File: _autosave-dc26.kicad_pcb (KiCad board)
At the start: 4 copper layers, 129.2 x 142.3 mm, 694 parts, among them J1 CONN_01X10, J2 CONN_01X10, J3 CONN_01X10, Q1 IRLB8721PBF, Y1 Crystal

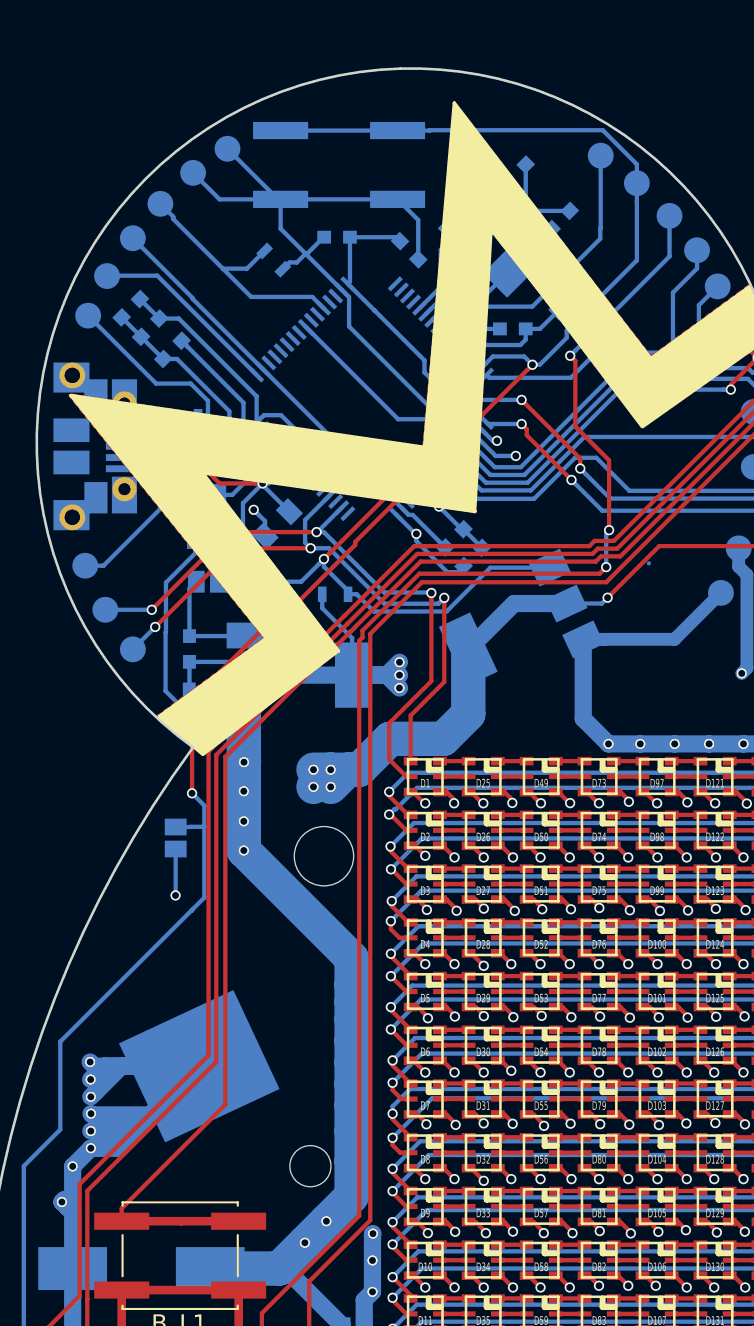
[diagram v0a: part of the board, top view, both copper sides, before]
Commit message: Name changes on silk
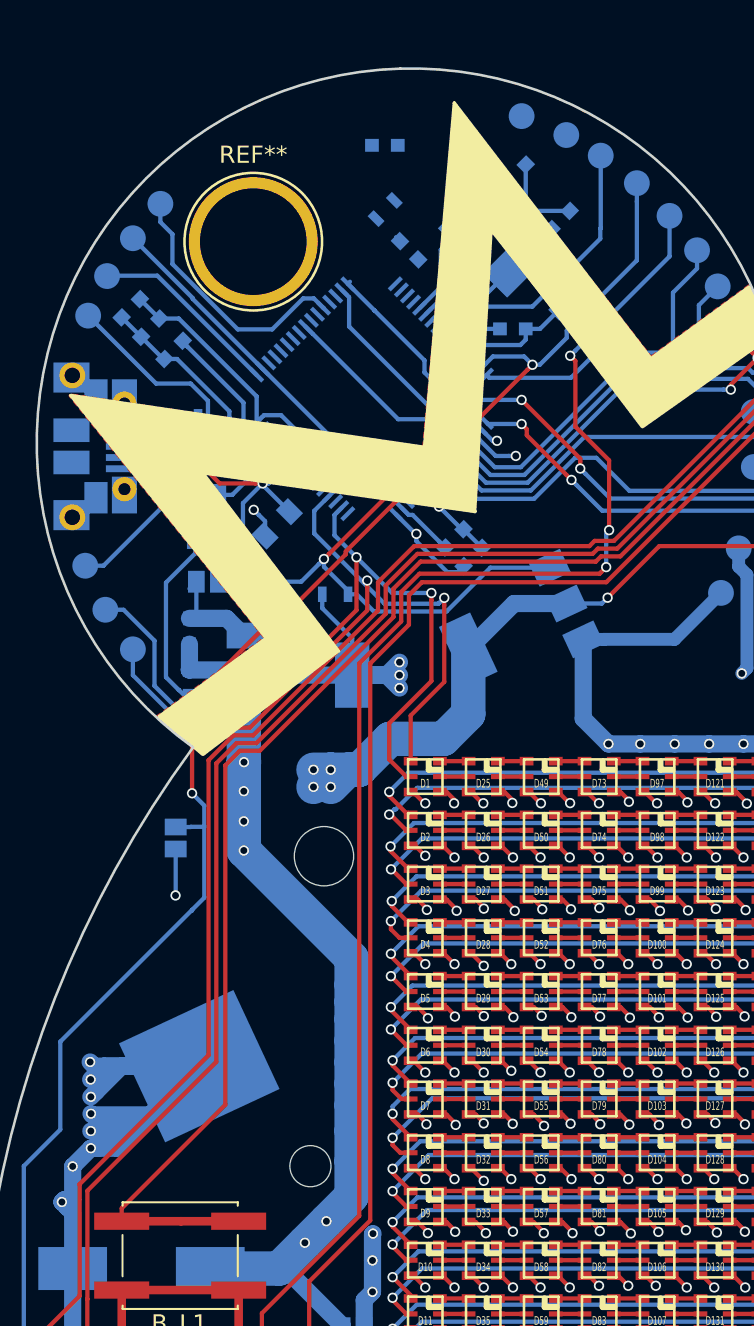
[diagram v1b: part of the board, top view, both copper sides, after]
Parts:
- removed SW_PWRON1: SW_SPST, Buttons_Switches_SMD:SW_SPST_EVQQ2
- added REF**: 1pin, custom-footprints:1pin-7mm, F.Cu at (126.5, 65.3)
- moved LGND1 19.7 mm to (144.7, 59.1)
- moved PGND1 19.4 mm to (142.1, 58.0)
- moved R14 7.12 mm to (134.2, 63.4), turned to 45 degrees
- moved C28 6.02 mm to (134.2, 59.7)
- moved C33 1.13 mm to (122.8, 91.0)
- moved C29 1.03 mm to (122.8, 88.0)
- moved C27 0.07 mm to (121.9, 71.6)
- turned NRST1 to 0 degrees
- renumbered TP-BATT-BUCK-ENABLE1 to BBEN1, TP-BTN-CLK1 to BCLK1, TP-BTN-DATA1 to BDATA1, TP-BATT-GND1 to BGND1, TP-BTN-GND1 to BGND2, TP-BATT-IN1 to BIN1, TP-BTN-LOAD1 to BLD1, TP-BOOT0 to BT0, JMP-BATT-BUCK-ENABLE1 to JBBEN1, JMP-LED-PWR-EN-BYP1 to JLEN1, JMP-LED-PWR-BYP1 to JLPWR1, JMP-USBID1 to JUID1, JMP-USBVCC1 to JUVCC1, TP-LED-CKI1 to LCKI1, TP-LED-PWR-EN1 to LEN1, TP-LED-GND1 to LGND1, TP-LED-SDI1 to LSDI1, TP-LED-VCC1 to LVCC1, TP-MPU6000-CS1 to MCS1, TP-MPU6000-INT1 to MINT1, TP-MPU6000-MISO1 to MMISO1, TP-MPU6000-MOSI1 to MMOSI1, TP-MPU6000-SCLK1 to MSCLK1, TP-NRST1 to NRST1, TP-PGM-GND1 to PGND1, TP-PGM-SWDCLK1 to SWDCLK1, TP-PGM-SWDIO1 to SWDIO1, TP-USBID1 to UID1
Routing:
- net GND: track 1146.3 -> 1111.8 mm
- net BATT-BUCK-ENABLE: track 146.2 -> 123.6 mm
- net LED-CKI: track 36.7 -> 45.7 mm
- net LED-SDI: track 36.3 -> 43.7 mm
- net +3V3: track 203.1 -> 197.8 mm
- net +5V: track 456.8 -> 452.7 mm
- net Net-(B_L4-Pad2): track 163.0 -> 163.6 mm
- net Net-(B_L3-Pad2): track 178.7 -> 179.3 mm
- net Net-(B_L1-Pad2): track 163.1 -> 163.8 mm
